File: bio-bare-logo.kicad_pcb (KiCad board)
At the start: 2 copper layers, 49.7 x 49.7 mm, 6 parts, among them X1 Badgelife_shitty_connector

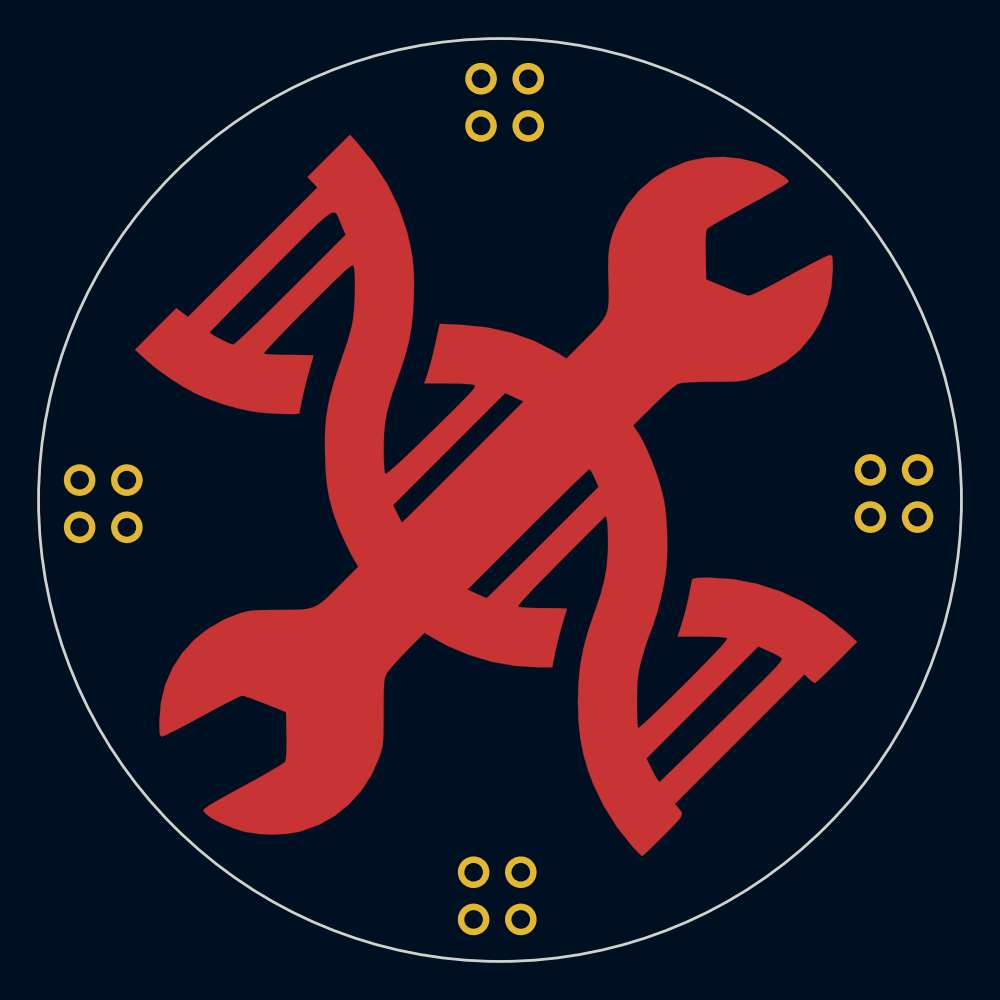
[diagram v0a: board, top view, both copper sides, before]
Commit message: add simple BioHacking Village artwork to add-on board
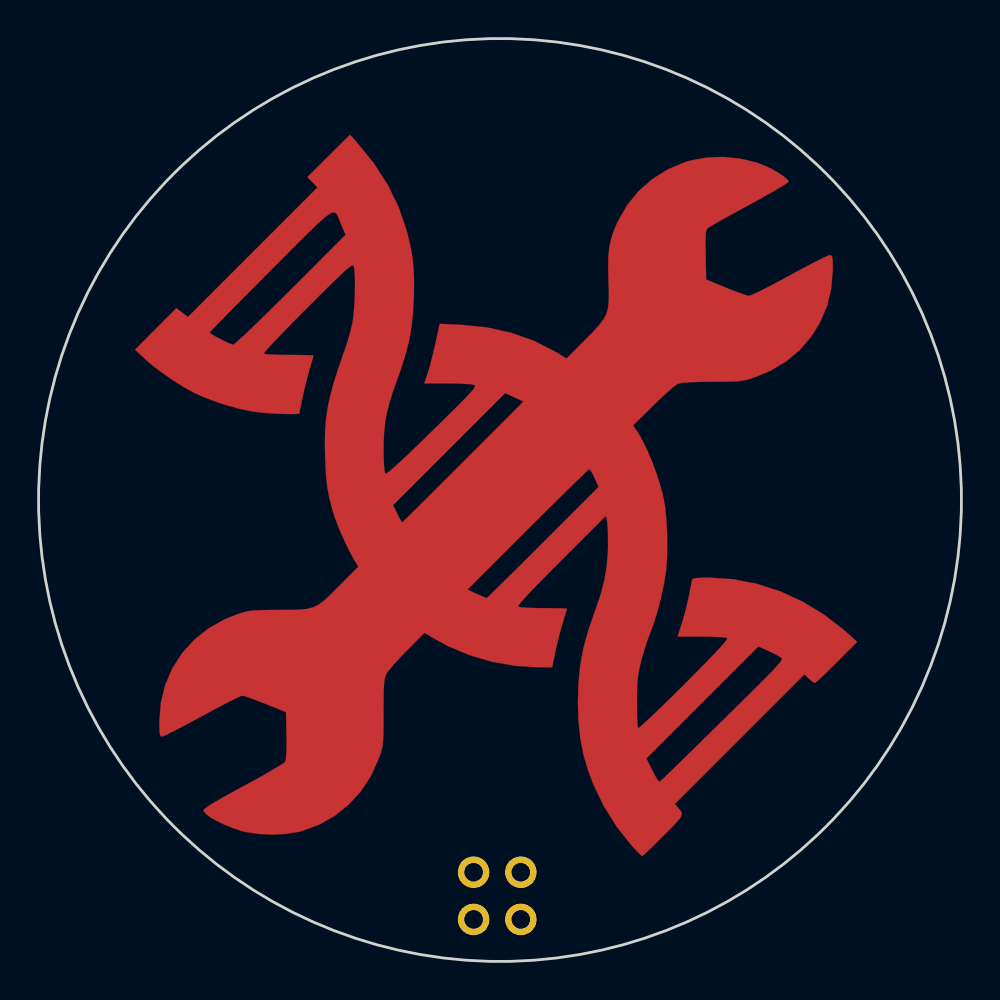
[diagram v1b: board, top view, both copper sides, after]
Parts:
- removed the X1 at (147.3, 135.8)
- removed the X1 at (168.3, 156.8)
- removed the X1 at (125.8, 157.3)
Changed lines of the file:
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@@
 (kicad_pcb (version 4) (host pcbnew 4.0.6+dfsg1-1)
   (general
-    (links 12)
-    (no_connects 12)
+    (links 0)
+    (no_connects 0)
     (area 94.116316 137.286666 171.450001 210.500001)
     (thickness 1.6)
@@
     (tracks 0)
     (zones 0)
-    (modules 6)
+    (modules 3)
     (nets 5)
   )
@@
     (add_net SDA)
   )
-  (module mrmeeseeks:Badgelife-Shitty-2x2 (layer B.Cu)
-    (at 147.35 135.75)
-    (descr "Through hole angled pin header, 2x02, 2.54mm pitch, 6mm pin length, double rows")
-    (tags "Through hole angled pin header THT 2x02 2.54mm double row")
-    (fp_text reference X1 (at 0 0) (layer B.Fab)
-      (effects (font (size 1 1) (thickness 0.15)) (justify mirror))
-    )
-    (fp_text value Badgelife_shitty_connector (at 0 -4.2) (layer B.Fab)
-      (effects (font (size 1 1) (thickness 0.15)) (justify mirror))
-    )
-    (fp_line (start -25 -9) (end 25 -9) (layer B.Fab) (width 0.1))
-    (fp_circle (center -2.54 2.54) (end -2.14 2.54) (layer B.SilkS) (width 0.15))
-    (fp_line (start -25 41) (end -25 -9) (layer B.Fab) (width 0.1))
-    (fp_line (start 25 41) (end 25 -9) (layer B.Fab) (width 0.1))
-    (fp_line (start -25 41) (end 25 41) (layer B.Fab) (width 0.1))
-    (pad 4 thru_hole circle (at 1.27 1.27) (size 1.7 1.7) (drill 1) (layers *.Cu *.Mask)
-      (net 3 SDA))
-    (pad 3 thru_hole oval (at 1.27 -1.27) (size 1.7 1.7) (drill 1) (layers *.Cu *.Mask)
-      (net 4 SCL))
-    (pad 1 thru_hole oval (at -1.27 1.27) (size 1.7 1.7) (drill 1) (layers *.Cu *.Mask)
-      (net 1 +3V3))
-    (pad 2 thru_hole oval (at -1.27 -1.27) (size 1.7 1.7) (drill 1) (layers *.Cu *.Mask)
-      (net 2 GND))
-  )
-  (module mrmeeseeks:Badgelife-Shitty-2x2 (layer B.Cu)
-    (at 168.3 156.8)
-    (descr "Through hole angled pin header, 2x02, 2.54mm pitch, 6mm pin length, double rows")
-    (tags "Through hole angled pin header THT 2x02 2.54mm double row")
-    (fp_text reference X1 (at 0 0) (layer B.Fab)
-      (effects (font (size 1 1) (thickness 0.15)) (justify mirror))
-    )
-    (fp_text value Badgelife_shitty_connector (at 0 -4.2) (layer B.Fab)
-      (effects (font (size 1 1) (thickness 0.15)) (justify mirror))
-    )
-    (fp_line (start -25 -9) (end 25 -9) (layer B.Fab) (width 0.1))
-    (fp_circle (center -2.54 2.54) (end -2.14 2.54) (layer B.SilkS) (width 0.15))
-    (fp_line (start -25 41) (end -25 -9) (layer B.Fab) (width 0.1))
-    (fp_line (start 25 41) (end 25 -9) (layer B.Fab) (width 0.1))
-    (fp_line (start -25 41) (end 25 41) (layer B.Fab) (width 0.1))
-    (pad 4 thru_hole circle (at 1.27 1.27) (size 1.7 1.7) (drill 1) (layers *.Cu *.Mask)
-      (net 3 SDA))
-    (pad 3 thru_hole oval (at 1.27 -1.27) (size 1.7 1.7) (drill 1) (layers *.Cu *.Mask)
-      (net 4 SCL))
-    (pad 1 thru_hole oval (at -1.27 1.27) (size 1.7 1.7) (drill 1) (layers *.Cu *.Mask)
-      (net 1 +3V3))
-    (pad 2 thru_hole oval (at -1.27 -1.27) (size 1.7 1.7) (drill 1) (layers *.Cu *.Mask)
-      (net 2 GND))
-  )
-  (module mrmeeseeks:Badgelife-Shitty-2x2 (layer B.Cu)
-    (at 125.75 157.35)
-    (descr "Through hole angled pin header, 2x02, 2.54mm pitch, 6mm pin length, double rows")
-    (tags "Through hole angled pin header THT 2x02 2.54mm double row")
-    (fp_text reference X1 (at 0 0) (layer B.Fab)
-      (effects (font (size 1 1) (thickness 0.15)) (justify mirror))
-    )
-    (fp_text value Badgelife_shitty_connector (at 0 -4.2) (layer B.Fab)
-      (effects (font (size 1 1) (thickness 0.15)) (justify mirror))
-    )
-    (fp_line (start -25 -9) (end 25 -9) (layer B.Fab) (width 0.1))
-    (fp_circle (center -2.54 2.54) (end -2.14 2.54) (layer B.SilkS) (width 0.15))
-    (fp_line (start -25 41) (end -25 -9) (layer B.Fab) (width 0.1))
-    (fp_line (start 25 41) (end 25 -9) (layer B.Fab) (width 0.1))
-    (fp_line (start -25 41) (end 25 41) (layer B.Fab) (width 0.1))
-    (pad 4 thru_hole circle (at 1.27 1.27) (size 1.7 1.7) (drill 1) (layers *.Cu *.Mask)
-      (net 3 SDA))
-    (pad 3 thru_hole oval (at 1.27 -1.27) (size 1.7 1.7) (drill 1) (layers *.Cu *.Mask)
-      (net 4 SCL))
-    (pad 1 thru_hole oval (at -1.27 1.27) (size 1.7 1.7) (drill 1) (layers *.Cu *.Mask)
-      (net 1 +3V3))
-    (pad 2 thru_hole oval (at -1.27 -1.27) (size 1.7 1.7) (drill 1) (layers *.Cu *.Mask)
-      (net 2 GND))
-  )
   (module badgelife_dev_board:wrench-neg-mask (layer F.Cu)
